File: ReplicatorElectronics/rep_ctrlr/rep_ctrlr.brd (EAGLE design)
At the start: 114.5 x 98.5 mm, 98 parts, among them IC1 MICROCHIP_PIC32MX7X5F256L-PF, IC2 MICROCHIP_MCP6001-LT, IC3 MICROCHIP_MCP6001-LT, IC4 MICROCHIP_MCP6001-LT, IC5 MICROCHIP_MCP6001-LT, J1 ATX24RH, J10 SBH11-PBPC-D07-ST-BK, J11 SBH11-PBPC-D07-ST-BK, J12 SBH11-PBPC-D07-ST-BK, J13 SBH11-PBPC-D07-ST-BK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

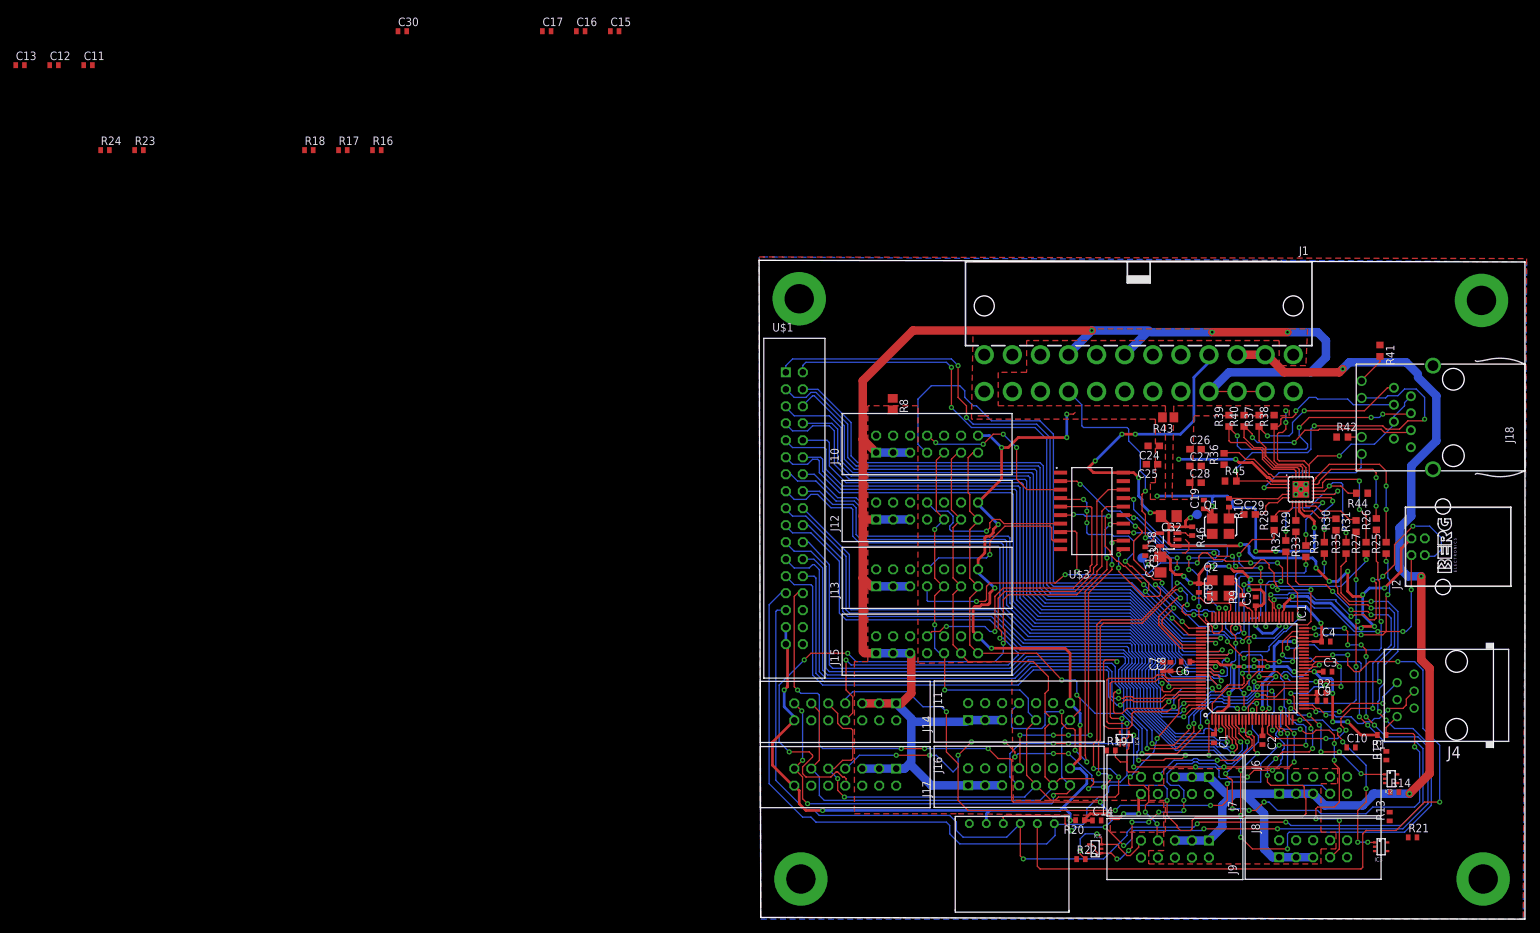
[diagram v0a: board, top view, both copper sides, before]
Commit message: 5/28/12: Preliminary placement and routing complete, need to clean up DRC errors.
~ 2 hrs.
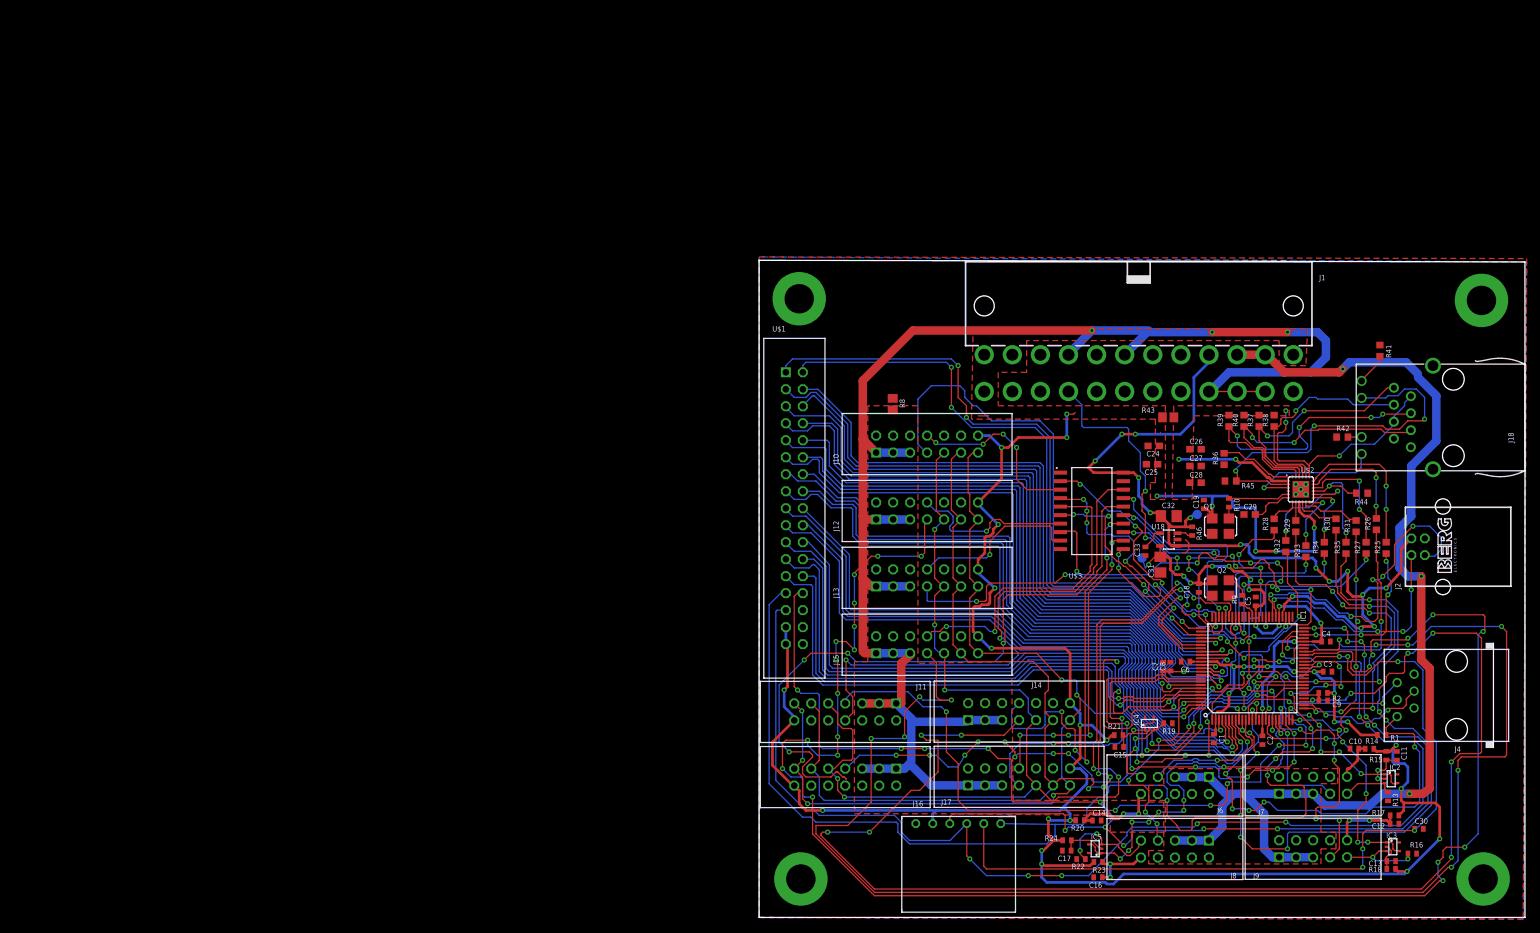
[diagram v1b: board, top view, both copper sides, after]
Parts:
- moved C13 237.0 mm to (94.5, 2.92)
- moved C12 230.3 mm to (95.0, 8.50)
- moved C11 221.2 mm to (95.3, 18.7), turned to 90 degrees
- moved R18 194.2 mm to (94.5, 1.75)
- moved C30 193.2 mm to (98.7, 7.75)
- moved R16 187.2 mm to (97.7, 4.03), turned to 180 degrees
- moved R17 186.1 mm to (95.0, 9.75)
- moved R23 178.6 mm to (50.7, 2.78), turned to 180 degrees
- moved R24 177.0 mm to (46.0, 6.03), turned to 180 degrees
- moved C16 148.3 mm to (50.7, 0.50), turned to 180 degrees
- moved C17 145.1 mm to (46.0, 4.50), turned to 180 degrees
- moved C15 130.9 mm to (53.8, 20.0), turned to 180 degrees
- moved R21 46.5 mm to (53.8, 21.8), turned to 180 degrees
- moved R19 9.45 mm to (61.1, 23.5), turned to 180 degrees
- moved J19 8.00 mm to (28.5, 3.45)
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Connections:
- net ENC2_CSN: now also IC1.42; no longer IC1.58
- net ENC4_CSN: now also IC1.28; no longer IC1.60
- net ENC5_CSN: now also IC1.43; no longer IC1.61
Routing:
- net ENC2_CSN: track 0.00 -> 255.3 mm, vias 0 -> 22
- net ENC5_CSN: track 0.00 -> 223.6 mm, vias 0 -> 10
- net ENC4_CSN: track 0.00 -> 213.8 mm, vias 0 -> 10
- net ENC_3_3V: track 220.4 -> 342.1 mm, vias 15 -> 23
- net N$11: track 0.00 -> 12.6 mm, vias 0 -> 2
- net N$12: track 0.00 -> 10.7 mm, vias 0 -> 2
- net N$20: track 0.00 -> 9.42 mm, vias 0 -> 2
- net SD_SP_MOSI: track 195.5 -> 204.3 mm
- net SP_CSN: track 115.8 -> 124.2 mm, vias 4 -> 6
- net SD_SP_SCK: track 174.8 -> 182.8 mm
- net N$9: track 0.00 -> 7.85 mm
- net N$21: track 0.00 -> 6.58 mm
- net N$14: track 0.00 -> 6.50 mm, vias 0 -> 2
- net N$18: track 0.00 -> 6.05 mm
- net N$13: track 0.00 -> 6.05 mm
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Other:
- board size 114.5 x 98.5 mm -> 114.5 x 98.2 mm

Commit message: 5/30/12: Preliminary layout finished! Ready for review by Alex.
~ 2 hrs.
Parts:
- added C20: 0.1u, resistor:C0402
- J4: value RJ11-2L-B -> (none); device con-tycoelectronics:RJ11-NO_SHIELD -> con-molex:22-23-2061
- moved J4 3.63 mm to (101.0, 29.4)
- moved R1 1.40 mm to (94.5, 21.8)
- moved 5V 0.46 mm to (65.4, 55.2)
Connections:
- removed net VCC: J4.2
- net +3V3: now also J4.2
- net 5V_USB: now also C20.1
- net DGND: now also C20.2
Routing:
- net 12V_HEAT: track 180.6 -> 200.1 mm, vias 3 -> 5
- net +3V3: track 127.1 -> 137.3 mm
- net PGEC: track 16.5 -> 23.8 mm, vias 3 -> 5
- net PGED: track 20.2 -> 25.7 mm
- net SERVO7: track 35.4 -> 40.8 mm
- net ENC2_CSN: track 255.3 -> 259.3 mm, vias 22 -> 20
- net MCLRN: track 67.4 -> 69.5 mm
- net 5V_USB: track 129.6 -> 127.8 mm, vias 15 -> 13
- net ETXD0: track 36.6 -> 38.2 mm
- net ENC5_CSN: track 223.6 -> 225.1 mm
- net SERVO2: track 44.0 -> 45.0 mm
- net DGND: track 3.77 -> 2.77 mm
- net SERVO6: track 37.2 -> 36.3 mm
- net SP_CSN: track 124.2 -> 123.5 mm
